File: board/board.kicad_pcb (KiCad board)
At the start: 2 copper layers, 21 x 13 mm, 11 parts, among them J1 003_power, J2 Conn_01x02_Male, J3 003_power, U1 TLV61220

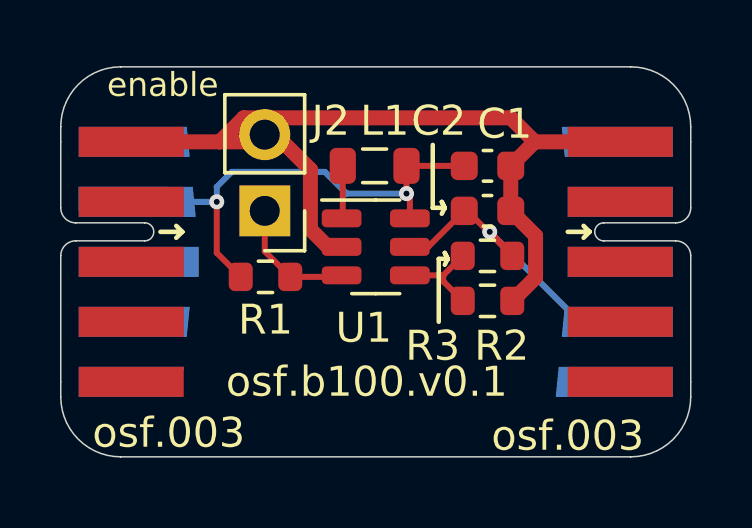
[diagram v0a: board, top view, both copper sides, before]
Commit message: moved components for better EMC
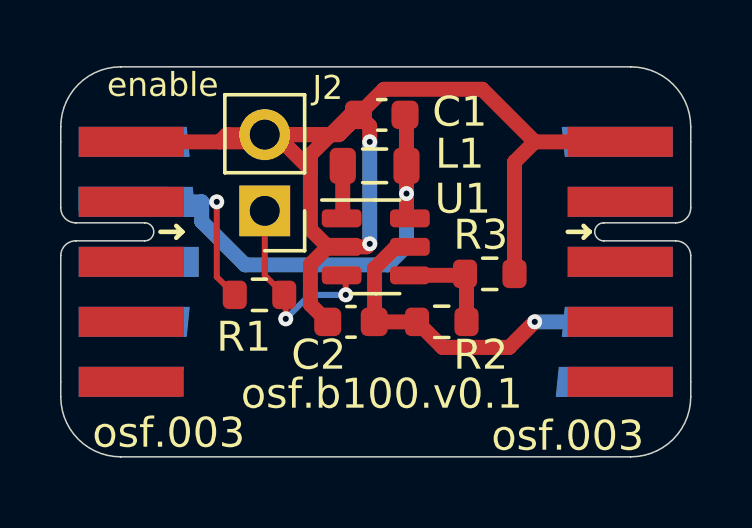
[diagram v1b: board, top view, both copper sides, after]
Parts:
- moved C2 5.86 mm to (149.7, 98.5), turned to 180 degrees
- moved C1 3.91 mm to (150.7, 91.6), turned to 180 degrees
- moved R2 2.68 mm to (152.7, 98.5), turned to 0 degrees
- moved R3 0.90 mm to (154.3, 96.9)
- moved R1 0.63 mm to (146.6, 97.6), turned to 0 degrees
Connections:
- net /implementation/3.3V renamed /step up/3.3V
- net Net-(L1-Pad2) renamed /step up/SW
- net Net-(R2-Pad2) renamed /step up/FB
- C1 pad 1: /implementation/in -> /step up/in
- J1 pad 7: /implementation/in -> /step up/in
- J2 pad 1: /implementation/EN -> /step up/EN
- L1 pad 1: /implementation/in -> /step up/in
- R1 pad 1: /implementation/EN -> /step up/in
- R1 pad 2: /implementation/in -> /step up/EN
- U1 pad 3: /implementation/EN -> /step up/EN
- U1 pad 6: /implementation/in -> /step up/in
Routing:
- net /step up/in: track 0.00 -> 21.8 mm, vias 0 -> 2
- net /implementation/in: track 17.0 -> 0.00 mm, vias 2 -> 0
- net GND: track 29.9 -> 43.6 mm, vias 0 -> 2
- net /step up/EN: track 0.00 -> 6.93 mm, vias 0 -> 2
- net /implementation/EN: track 4.29 -> 0.00 mm
- net /step up/3.3V: track 11.2 -> 12.1 mm

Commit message: changed input to battery cell connector
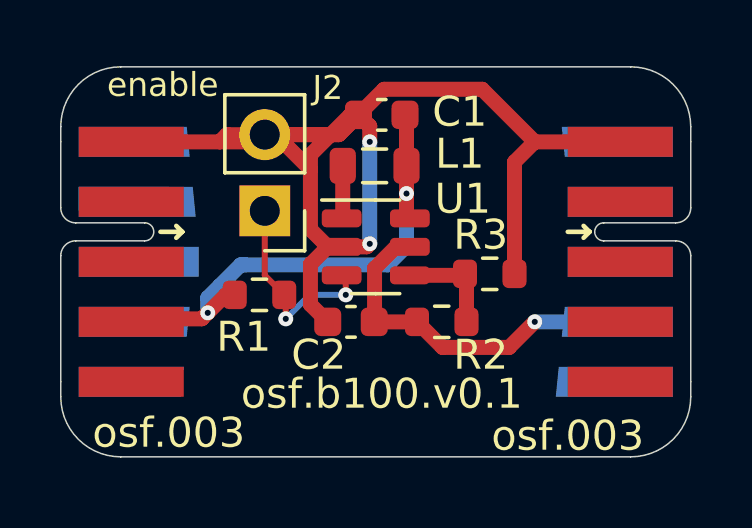
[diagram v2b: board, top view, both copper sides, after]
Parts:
- J1: value 003_power -> 022_battery_cells
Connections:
- J1 pad 10: unconnected-(J1-Pad10) -> (no net)
- J1 pad 4: unconnected-(J1-Pad4) -> /step up/in
- J1 pad 7: /step up/in -> (no net)
- J1 pad 8: unconnected-(J1-Pad8) -> (no net)
- J1 pad 9: unconnected-(J1-Pad9) -> (no net)
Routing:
- net /step up/in: track 21.8 -> 18.7 mm
